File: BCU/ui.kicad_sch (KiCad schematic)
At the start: 16 parts

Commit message: Make rough component placement for evaluating missing 3D
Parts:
- SW1, SW2, SW3, SW4, SW5: renamed from SW?; footprint (none) -> coilchain-switch:TS-1101-C-W
- gave numbers to parts that had none: 11

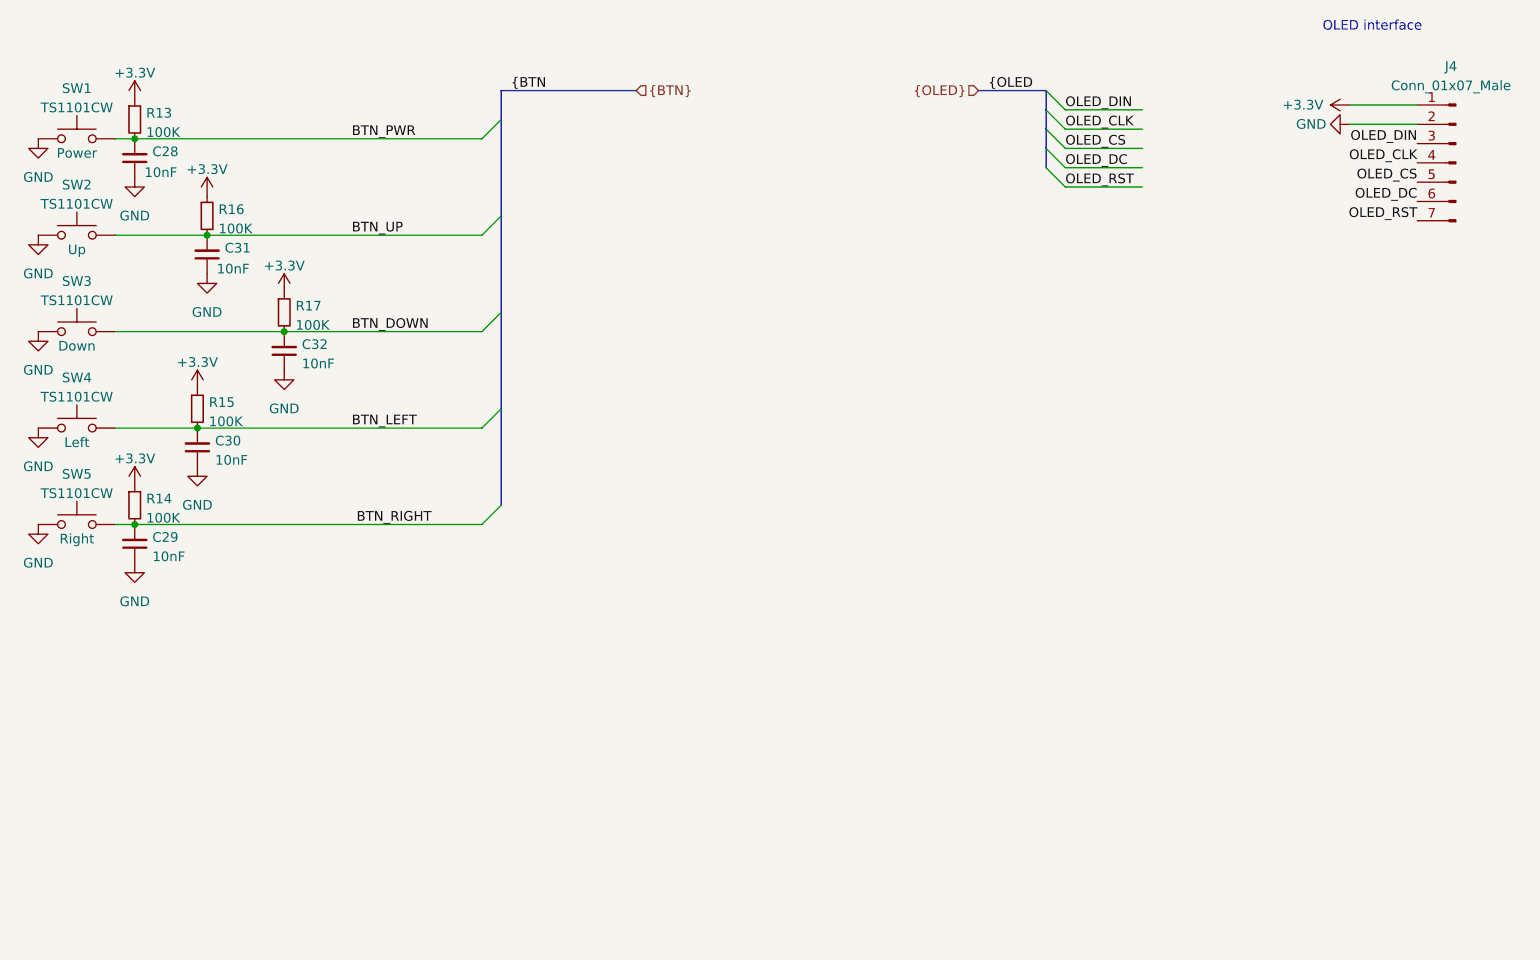
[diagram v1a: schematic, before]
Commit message: Added power enable logic
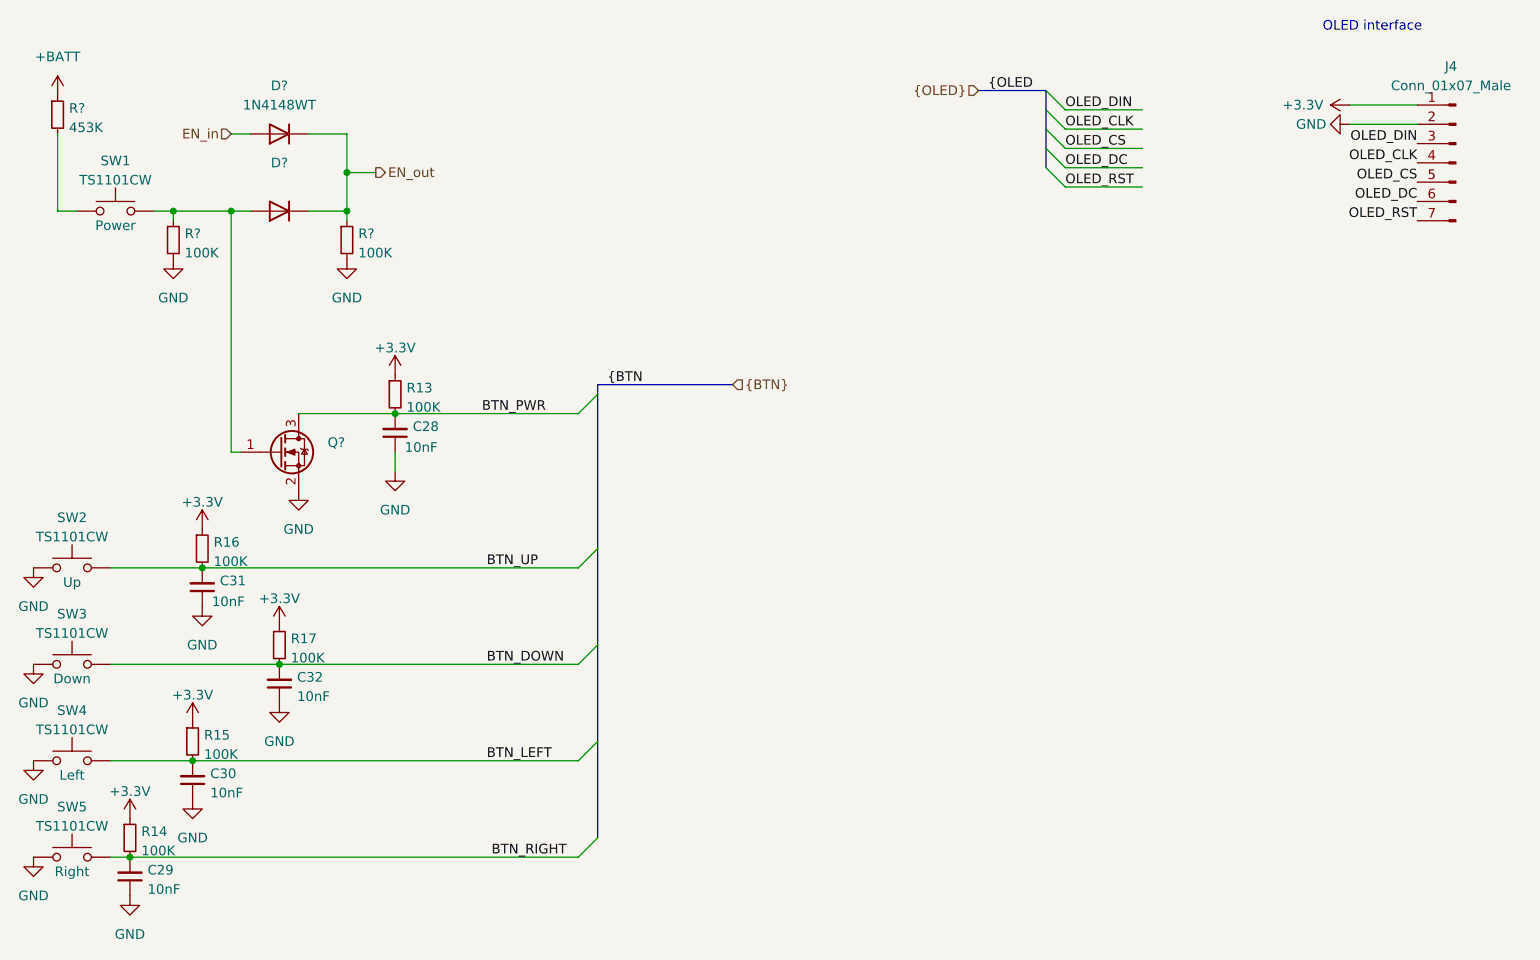
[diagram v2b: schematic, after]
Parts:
- added D?: 1N4148WT, Diode_SMD:D_SOD-523, symbol Diode:1N4148WT
- added D?: (no value), symbol Diode:1N4148WT
- added Q?: (no value), symbol Transistor_FET:2N7002
- added R? (x2): 100K, Resistor_SMD:R_0402_1005Metric_Pad0.72x0.64mm_HandSolder, symbol Device:R_Small
- added R?: 453K, Resistor_SMD:R_0402_1005Metric_Pad0.72x0.64mm_HandSolder, symbol Device:R_Small
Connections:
- net BTN_PWR: now also Q?.3 (D); no longer SW1.2
- net GND: now also Q?.2 (S), R?.2, R?.2; no longer SW1.1
- new net: D?.2 (A), Q?.1 (G), R?.1, SW1.2
- new net: R?.2, SW1.1
- new net +BATT: R?.1
- new net EN_in: D?.2 (A)
- new net EN_out: D?.1 (K), D?.1 (K), R?.1
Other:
- moved on the sheet: C28, C29, C30, C31, C32, R13, R14, R15, R16, R17, SW1, SW2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
